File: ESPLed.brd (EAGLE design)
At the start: 70 x 70 mm, 20 parts, among them IC1 TLC59711

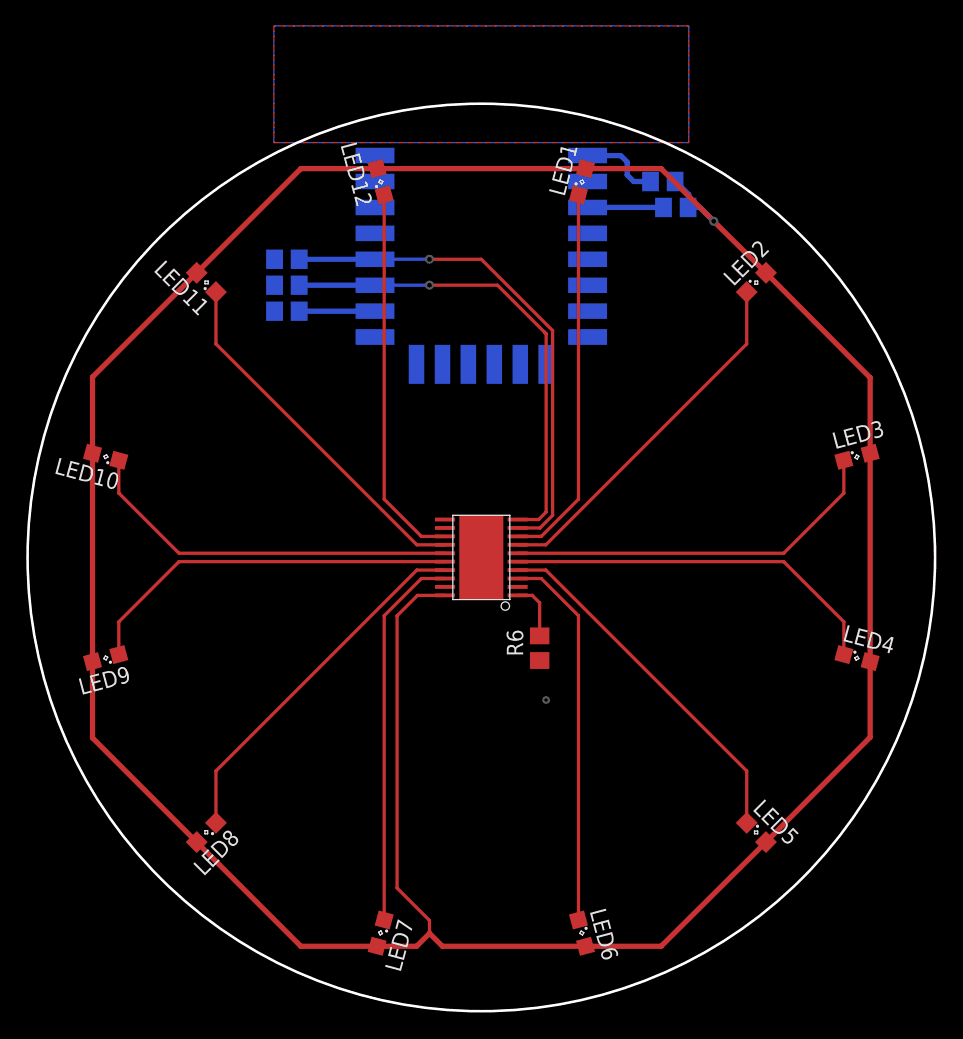
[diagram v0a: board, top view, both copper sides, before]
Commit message: buttons, usb
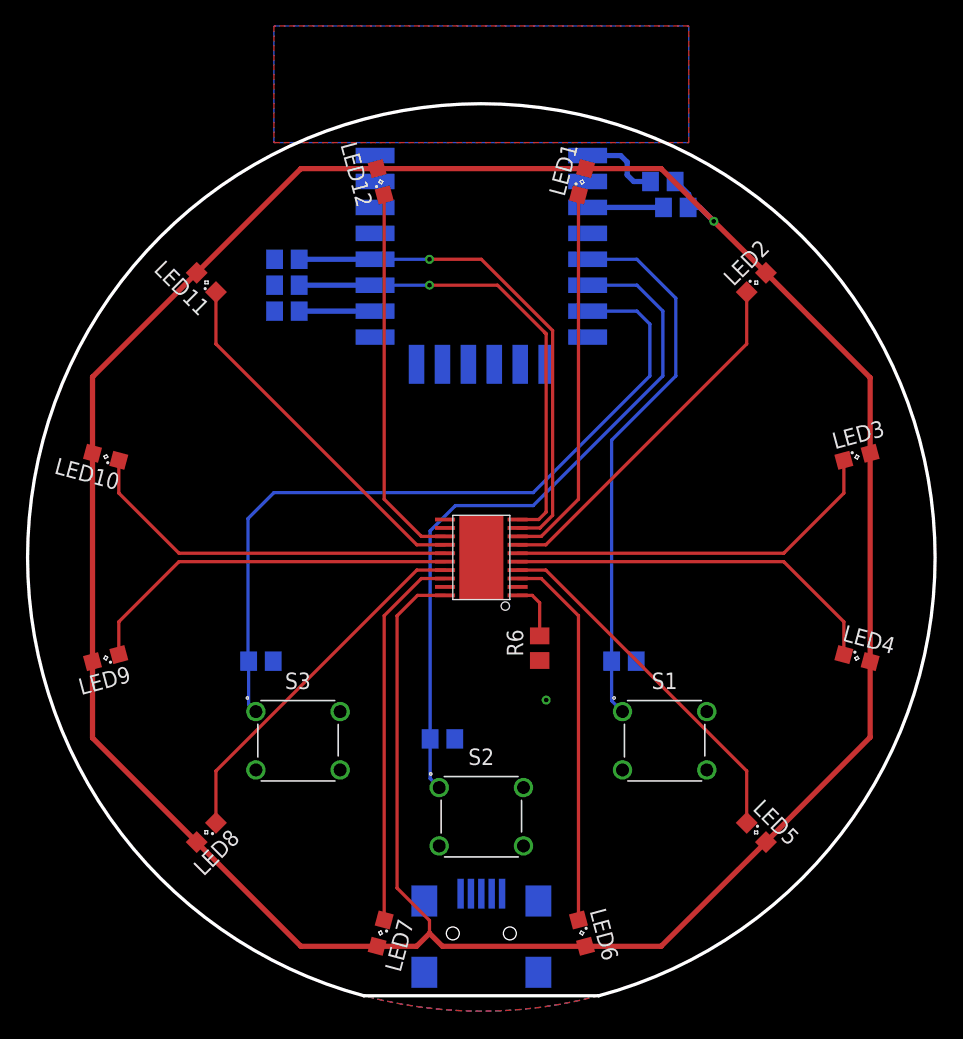
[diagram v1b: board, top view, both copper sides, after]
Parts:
- added CN1: (no value), adafruit:USB-MINIB
- added R7, R8, R9: 10k, resistor:R0805
- added S1, S2, S3: (no value), Wurth_Elektronik_Electromechanic_Switch_rev17b:4301X6XXX7X6
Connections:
- new net VBUS: CN1.VBUS
- net +3V3: now also R7.2, R8.2, R9.2
- net GND: now also CN1.GND, S1.2, S2.2, S3.2
- net GPIO12: now also R8.1, S2.1
- net GPIO13: now also R9.1, S3.1
- net GPIO14: now also R7.1, S1.1
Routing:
- net GPIO13: track 0.00 -> 59.9 mm
- net GPIO12: track 0.00 -> 54.6 mm
- net GPIO14: track 0.00 -> 42.3 mm
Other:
- board size 70 x 70 mm -> 70 x 68.8 mm
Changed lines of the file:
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@@
 <board>
 <plain>
-<circle x="0" y="0" radius="35" width="0.2" layer="20"/>
+<wire x1="-9.059" y1="-33.81" x2="9.059" y2="-33.81" width="0.254" layer="20" curve="-330"/>
+<wire x1="-9.059" y1="-33.81" x2="9.059" y2="-33.81" width="0.254" layer="20"/>
 </plain>
 <attributes>
@@
 <element name="IC1" library="adafruit" library_urn="urn:adsk.eagle:library:420" package="HTSSOP20DAP" value="TLC59711" x="0" y="0" rot="R90"/>
 <element name="R6" library="resistor" library_urn="urn:adsk.eagle:library:348" package="R0805" value="1.98k" x="4.5" y="-7" rot="R90"/>
+<element name="S1" library="Wurth_Elektronik_Electromechanic_Switch_rev17b" library_urn="urn:adsk.eagle:library:443" package="4301X6XXX7X6" value="" x="14.14" y="-14.14"/>
+<element name="S2" library="Wurth_Elektronik_Electromechanic_Switch_rev17b" library_urn="urn:adsk.eagle:library:443" package="4301X6XXX7X6" value="" x="0" y="-20"/>
+<element name="S3" library="Wurth_Elektronik_Electromechanic_Switch_rev17b" library_urn="urn:adsk.eagle:library:443" package="4301X6XXX7X6" value="" x="-14.14" y="-14.14"/>
+<element name="R7" library="resistor" library_urn="urn:adsk.eagle:library:348" package="R0805" value="10k" x="11" y="-8" rot="MR180"/>
+<element name="R8" library="resistor" library_urn="urn:adsk.eagle:library:348" package="R0805" value="10k" x="-3" y="-14" rot="MR180"/>
+<element name="R9" library="resistor" library_urn="urn:adsk.eagle:library:348" package="R0805" value="10k" x="-17" y="-8" rot="MR180"/>
+<element name="CN1" library="adafruit" library_urn="urn:adsk.eagle:library:420" package="USB-MINIB" value="" x="0" y="-30" rot="MR0"/>
 </elements>
 <signals>
@@
 <wire x1="-3.992221875" y1="-29" x2="-3" y2="-29.992221875" width="0.4064" layer="1"/>
 <wire x1="-4" y1="-28" x2="-4" y2="-29" width="0.254" layer="1"/>
+<contactref element="R7" pad="2"/>
+<contactref element="R8" pad="2"/>
+<contactref element="R9" pad="2"/>
 <wire x1="15.95" y1="27" x2="8.2" y2="17" width="0" layer="19" extent="16-16"/>
 <wire x1="-15.95" y1="21" x2="-21.955459375" y2="21.955459375" width="0" layer="19" extent="1-16"/>
 <wire x1="-15.95" y1="23" x2="-15.95" y2="21" width="0" layer="19" extent="16-16"/>
+<wire x1="-16.05" y1="-8" x2="-6.5" y2="-4.5" width="0" layer="19" extent="1-16"/>
+<wire x1="-2.05" y1="-14" x2="-6.5" y2="-4.5" width="0" layer="19" extent="1-16"/>
+<wire x1="11.95" y1="-8" x2="-2.05" y2="-14" width="0" layer="19" extent="16-16"/>
 </signal>
 <signal name="GND">
@@
 </polygon>
 <contactref element="IC1" pad="2"/>
-<via x="5" y="-11" extent="1-16" drill="0.25"/>
+<via x="5" y="-11" extent="1-16" drill="0.35"/>
 <contactref element="R6" pad="1"/>
+<contactref element="S1" pad="2"/>
+<contactref element="S2" pad="2"/>
+<contactref element="S3" pad="2"/>
+<contactref element="CN1" pad="GND"/>
+<wire x1="-17.39" y1="-16.39" x2="-1.6" y2="-25.936" width="0" layer="19" extent="1-1"/>
+<wire x1="-3.25" y1="-22.25" x2="-17.39" y2="-16.39" width="0" layer="19" extent="1-1"/>
+<wire x1="5" y1="-11" x2="-3.25" y2="-22.25" width="0" layer="19" extent="1-1"/>
+<wire x1="4.5" y1="-7.95" x2="5" y2="-11" width="0" layer="19" extent="1-1"/>
+<wire x1="2.8" y1="-2.275" x2="4.5" y2="-7.95" width="0" layer="19" extent="1-1"/>
+<wire x1="10.89" y1="-16.39" x2="5" y2="-11" width="0" layer="19" extent="1-1"/>
+<wire x1="-8.2" y1="17" x2="2.8" y2="-2.275" width="0" layer="19" extent="1-16"/>
+<wire x1="-15.95" y1="19" x2="-8.2" y2="17" width="0" layer="19" extent="16-16"/>
 </signal>
 <signal name="GPIO13">
 <contactref element="U1" pad="GPIO13"/>
+<contactref element="S3" pad="1"/>
+<contactref element="R9" pad="1"/>
+<wire x1="-17.95" y1="-8" x2="-17.95" y2="-11.33" width="0.254" layer="16"/>
+<wire x1="-17.95" y1="-11.33" x2="-17.39" y2="-11.89" width="0.254" layer="16"/>
+<wire x1="8.2" y1="19" x2="12" y2="19" width="0.254" layer="16"/>
+<wire x1="12" y1="19" x2="13" y2="18" width="0.254" layer="16"/>
+<wire x1="13" y1="18" x2="13" y2="14" width="0.254" layer="16"/>
+<wire x1="13" y1="14" x2="4" y2="5" width="0.254" layer="16"/>
+<wire x1="4" y1="5" x2="-16" y2="5" width="0.254" layer="16"/>
+<wire x1="-16" y1="5" x2="-18" y2="3" width="0.254" layer="16"/>
+<wire x1="-18" y1="3" x2="-18" y2="-7.95" width="0.254" layer="16"/>
+<wire x1="-18" y1="-7.95" x2="-17.95" y2="-8" width="0.254" layer="16"/>
 </signal>
 <signal name="GPIO12">
 <contactref element="U1" pad="GPIO12"/>
+<contactref element="S2" pad="1"/>
+<contactref element="R8" pad="1"/>
+<wire x1="-3.95" y1="-17.05" x2="-3.95" y2="-14" width="0.254" layer="16"/>
+<wire x1="-3.95" y1="-17.05" x2="-3.25" y2="-17.75" width="0.254" layer="16"/>
+<wire x1="-3.95" y1="-14" x2="-3.95" y2="2.05" width="0.254" layer="16"/>
+<wire x1="-3.95" y1="2.05" x2="-2" y2="4" width="0.254" layer="16"/>
+<wire x1="-2" y1="4" x2="4" y2="4" width="0.254" layer="16"/>
+<wire x1="4" y1="4" x2="14" y2="14" width="0.254" layer="16"/>
+<wire x1="14" y1="14" x2="14" y2="19" width="0.254" layer="16"/>
+<wire x1="14" y1="19" x2="12" y2="21" width="0.254" layer="16"/>
+<wire x1="12" y1="21" x2="8.2" y2="21" width="0.254" layer="16"/>
 </signal>
 <signal name="GPIO14">
 <contactref element="U1" pad="GPIO14"/>
+<contactref element="S1" pad="1"/>
+<contactref element="R7" pad="1"/>
+<wire x1="10.05" y1="-11.05" x2="10.05" y2="-8" width="0.254" layer="16"/>
+<wire x1="10.05" y1="-11.05" x2="10.89" y2="-11.89" width="0.254" layer="16"/>
+<wire x1="10.05" y1="-8" x2="10.05" y2="9.05" width="0.254" layer="16"/>
+<wire x1="10.05" y1="9.05" x2="15" y2="14" width="0.254" layer="16"/>
+<wire x1="15" y1="14" x2="15" y2="20" width="0.254" layer="16"/>
+<wire x1="15" y1="20" x2="12" y2="23" width="0.254" layer="16"/>
+<wire x1="12" y1="23" x2="8.2" y2="23" width="0.254" layer="16"/>
 </signal>
 <signal name="GPIO16">
@@
 <wire x1="4.5" y1="-3.5" x2="3.925" y2="-2.925" width="0.254" layer="1"/>
 </signal>
+<signal name="VBUS">
+<contactref element="CN1" pad="VBUS"/>
+</signal>
 </signals>

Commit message: lipo charging
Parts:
- added C1, C2: 12pF, resistor:C0805
- added C4, C5, C7: 10µF, resistor:C0805
- added C6: 1µF, resistor:C0805
- added D4: MBR120, microbuilder:SOD-123
- added IC2: MCP73831/OT, adafruit:SOT23-5L
- added LED13: (no value), led:SML0805
- added Q1: 12MHz, JonasLib:CX5032GB
- added Q3: DMG3415U, microbuilder:SOT23-R
- added R10: 2k, resistor:R0805
- added R11: 680, resistor:R0805
- added R13, R14: 100k, resistor:R0805
- added U$1: CH340G, ch340g:SOIC16
- added U3: AP2112-3.3, microbuilder:SOT23-5
- added X1: JSTPH, microbuilder:JSTPH2
- moved CN1 42.4 mm to (30.0, 0.00), turned to 270 degrees
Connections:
- net N$1 renamed IREF
- net N$8 renamed GPIO5
- removed net VCC: IC1.19
- new net IN: C4.2, D4.C, Q3.2, R13.1, U3.1
- new net N$1: LED13.C, R11.1
- new net PROG: IC2.5, R10.1
- new net STAT: IC2.1, R11.2
- new net USB_D+: CN1.D+, U$1.5
- new net USB_D-: CN1.D-, U$1.6
- new net USB_RX: U$1.3, U1.TXD0
- new net USB_TX: U$1.2, U1.RXD0
- new net VBAT: IC2.3, Q3.3, X1.2
- new net VREG_EN: R13.2, U3.3
- new net XI: C2.2, Q1.P$1, U$1.7
- new net XO: C1.2, Q1.P$2, U$1.8
- net +3V3: now also C5.2, C6.2, C7.2, IC1.19, U$1.16, U$1.4, U3.5
- net GND: now also C1.1, C2.1, C4.1, C5.1, C6.1, C7.1, IC2.2, R10.2, R14.1, U$1.1, U3.2, X1.1
- net VBUS: now also D4.A, IC2.4, LED13.A, Q3.1, R14.2
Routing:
- net IN: track 0.00 -> 72.3 mm
- net +3V3: track 237.8 -> 291.0 mm, vias 1 -> 8
- net USB_RX: track 0.00 -> 45.3 mm, vias 0 -> 4
- net USB_TX: track 0.00 -> 42.2 mm, vias 0 -> 4
- net VBUS: track 0.00 -> 38.8 mm, vias 0 -> 1
- net PROG: track 0.00 -> 22.2 mm
- net STAT: track 0.00 -> 17.2 mm, vias 0 -> 2
- net VBAT: track 0.00 -> 14.0 mm
- net USB_D+: track 0.00 -> 11.0 mm
- net N$1: track 0.00 -> 11.0 mm, vias 0 -> 1
- net USB_D-: track 0.00 -> 9.46 mm
- net XO: track 0.00 -> 8.97 mm
- net XI: track 0.00 -> 8.94 mm
- net LED8: track 28.1 -> 34.5 mm
- net LED5: track 28.1 -> 34.5 mm
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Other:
- board size 70 x 68.8 mm -> 68.8 x 70 mm
